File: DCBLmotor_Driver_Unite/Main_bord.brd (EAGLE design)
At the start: 160 x 100 mm, 50 parts, among them CN1 DF11-16DP-2DSA, CN2 DF11-16DP-2DSA, CN3 DF11-4DS-2C, CN4 HIF3FC-10PA-2.54DSA(71), CN5 HIF3FC-10PA-2.54DSA(71), IC1 TMPM370FYFG, IC2 MCP2561FD-E/MF, IC3 AM26C32CD, IC4 AM26C32CD, SW1 CVS-02TB

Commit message: Mount Encoder parts
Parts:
- moved DC11 6.19 mm to (67.8, 65.2)
- moved CN4 5.95 mm to (72.0, 68.8)
- moved CN5 5.80 mm to (72.0, 88.9)
- moved DC12 5.80 mm to (67.8, 85.3)
- moved R2 1.58 mm to (9.65, 72.2), turned to 180 degrees
- moved RA1 1.50 mm to (11.7, 80.0)
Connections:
- net ENC_A-1: now also IC3.3
- net ENC_A-2: now also IC4.3
- net ENC_B-1: now also IC3.5
- net ENC_B-2: now also IC4.5
- net ENC_Z-1: now also IC3.11
- net ENC_Z-2: now also IC4.11
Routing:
- net +5V: track 128.2 -> 78.9 mm, vias 10 -> 9
- net N$36: track 20.2 -> 13.5 mm
- net 1_I2: track 19.7 -> 13.4 mm
- net 2_B1: track 11.8 -> 6.06 mm
- net 1_B1: track 11.5 -> 5.96 mm
- net 2_B2: track 15.2 -> 9.84 mm
- net 1_B2: track 14.0 -> 9.14 mm
- net 2_A2: track 11.4 -> 7.58 mm
- net DIP8: track 31.5 -> 28.4 mm
- net 1_A1: track 7.79 -> 4.81 mm
- net 2_A1: track 7.57 -> 4.60 mm
- net 1_A2: track 10.7 -> 7.90 mm
- net N$35: track 12.8 -> 10.4 mm
- net 1_I1: track 12.6 -> 10.3 mm
- net DIP4: track 21.6 -> 23.9 mm
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
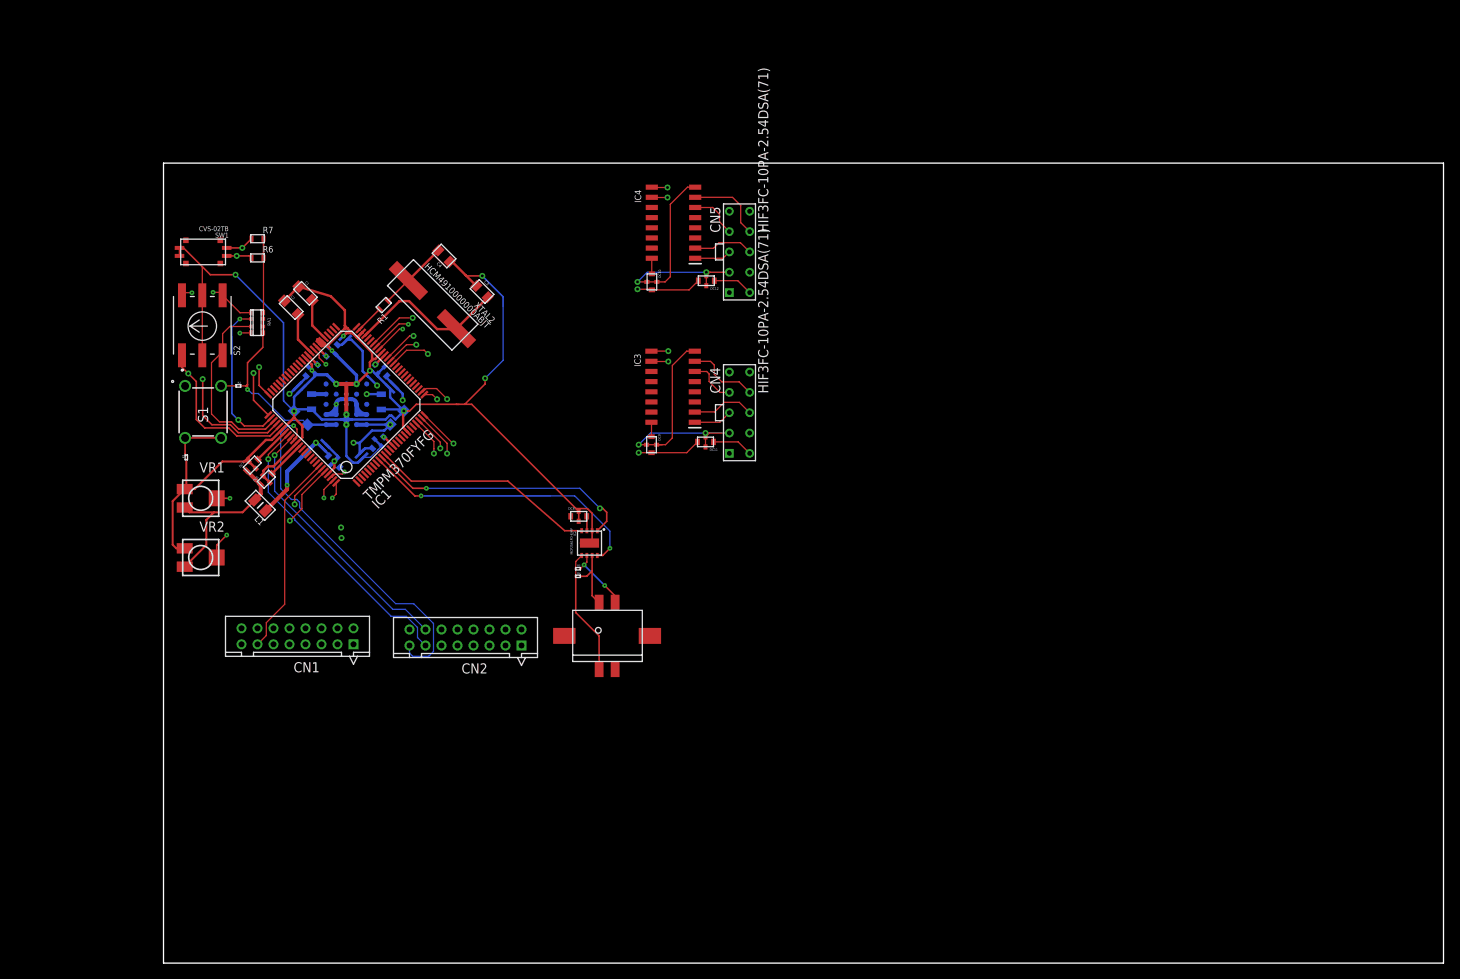
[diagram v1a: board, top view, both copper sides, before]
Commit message: Mount new parts
mount 
holl conecter
change
reset switch
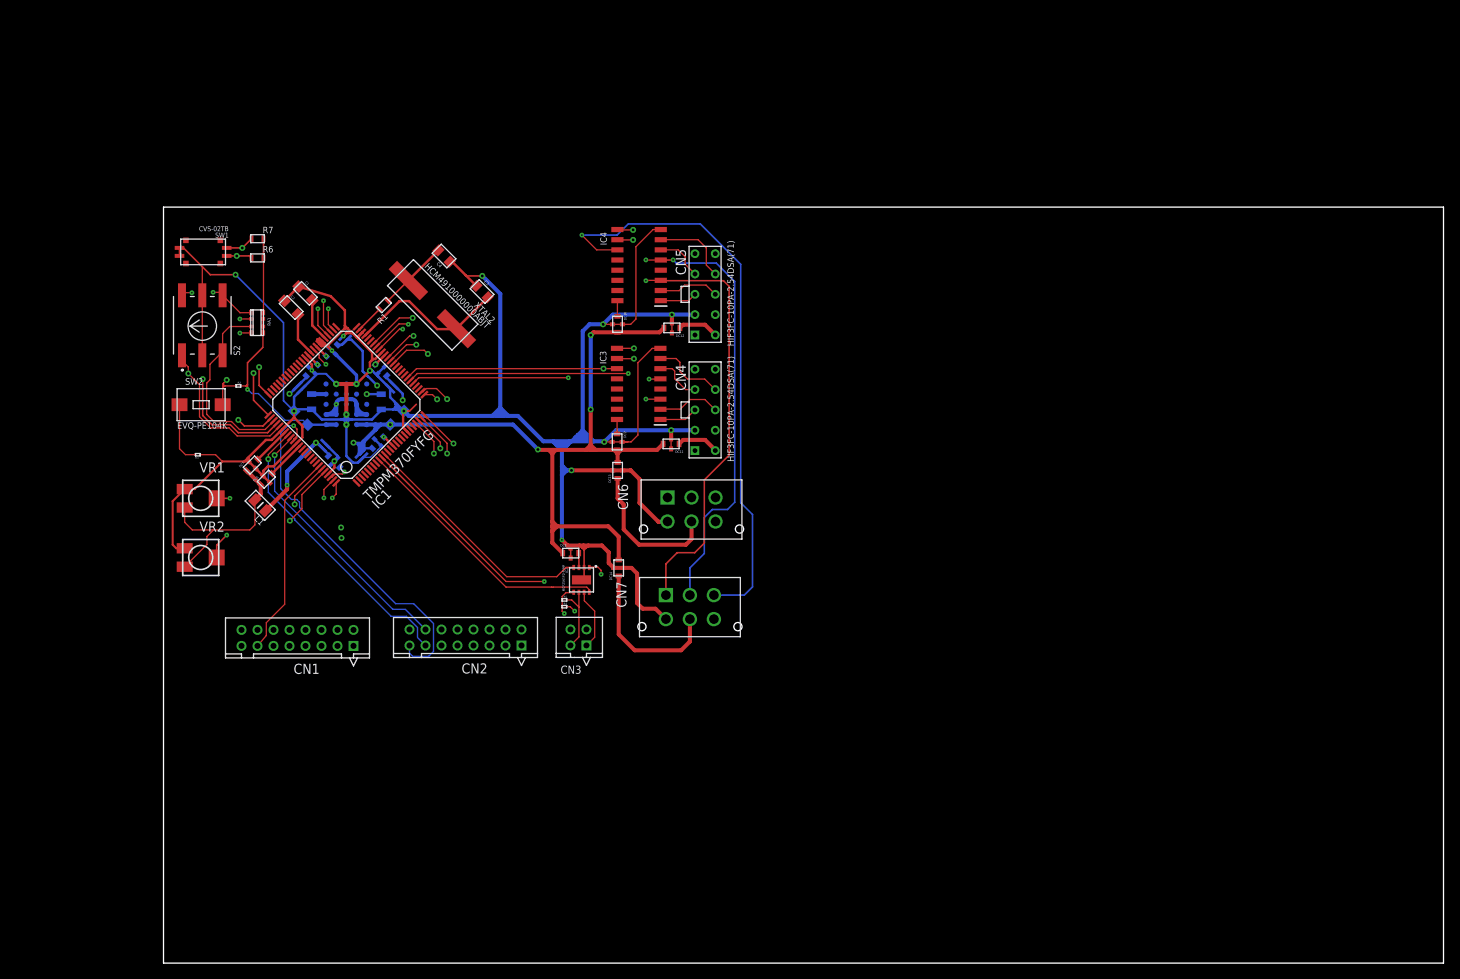
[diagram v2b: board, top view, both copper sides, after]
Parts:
- removed S1: 1825910-6, 1825910-6:1825910-6
- added CN6, CN7: 0430450612, Molex:0430450612
- added DC13, DC14: YFF21PC, TDK:YFF21PC
- added SW2: EVQ-PE104K, Panasonic:EVQ
- CN3: value DF11-4DS-2C -> DF11-4DP-2DSR; device Hirose:DF11-4DS-2C -> Hirose:DF11_4DP-2D
- moved DC12 7.30 mm to (63.5, 79.4)
- moved CN5 6.82 mm to (67.7, 83.6)
- moved DC10 6.82 mm to (56.8, 79.8)
- moved IC4 6.82 mm to (59.5, 87.2)
- moved DC8 4.71 mm to (50.9, 51.2)
- moved IC2 4.71 mm to (52.2, 47.9)
- moved IC3 4.31 mm to (59.4, 72.4)
- moved CN4 4.31 mm to (67.7, 69.2)
- moved DC9 4.31 mm to (56.7, 65.2)
- moved DC11 4.31 mm to (63.5, 64.9)
- moved R5 4.25 mm to (50.4, 45.4)
- moved R4 4.16 mm to (50.4, 44.5)
- moved CN3 3.55 mm to (51.9, 40.9), turned to 0 degrees
- moved R3 1.15 mm to (4.00, 63.5), turned to 0 degrees
- moved CN1 0.20 mm to (23.8, 39.6)
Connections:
- new net N$32: CN6.P$5, DC13.P$2
- new net N$33: CN7.P$5, DC14.P$2
- net +5V: now also DC13.P$1, DC14.P$1
- net ENC_A-1: now also CN6.P$1
- net ENC_A-2: now also CN7.P$1
- net ENC_B-1: now also CN6.P$2
- net ENC_B-2: now also CN7.P$2
- net ENC_Z-1: now also CN6.P$3
- net ENC_Z-2: now also CN7.P$3
- net GND: now also CN6.P$4, CN7.P$4, DC13.GND1, DC13.GND2, DC14.GND1, DC14.GND2
- net N$12: now also SW2.P$1; no longer S1.3, S1.4
- net RESET: now also SW2.P$2; no longer S1.2
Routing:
- net ENC_Z-2: track 0.00 -> 116.8 mm, vias 0 -> 2
- net ENC_B-2: track 0.00 -> 105.2 mm, vias 0 -> 3
- net ENC_A-2: track 0.00 -> 103.6 mm, vias 0 -> 2
- net +5V: track 78.9 -> 157.7 mm, vias 9 -> 10
- net GND: track 322.9 -> 399.6 mm, vias 13 -> 14
- net ENC_Z-1: track 0.00 -> 55.6 mm, vias 0 -> 1
- net ENC_B-1: track 0.00 -> 51.3 mm, vias 0 -> 2
- net ENC_A-1: track 0.00 -> 46.7 mm, vias 0 -> 2
- net N$33: track 0.00 -> 20.3 mm
- net N$32: track 0.00 -> 18.4 mm
- net SPLT: track 15.8 -> 7.59 mm, vias 0 -> 1
- net CANH: track 8.02 -> 14.0 mm, vias 0 -> 1
- net STBY: track 36.6 -> 33.3 mm, vias 2 -> 0
- net RESET: track 19.2 -> 22.5 mm, vias 1 -> 2
- net TX0: track 33.7 -> 36.6 mm
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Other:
- board size 160 x 100 mm -> 160 x 94.5 mm

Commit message: Version1 per finshed
Per complete Version1
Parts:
- removed XTAL2: HCM4910000000ABJT, Citizen:HCM49
- added 0R1, 0R2: 5106, Keystone:5106JUMP_0805
- added C5: T356L107K016AT, KEMET:T356
- added CN10: (no value), jst-xh:B2B-XH-A
- added CN8: BM11B-SRSS-TB, JST:BM11B-SRSS-TB
- added CN9: (no value), jst-xh:B4B-XH-A
- added CR10, CR11, CR12, CR5, CR6, CR7, CR8: NSI50010YT1G, ON Semiconductor:SOD-123
- added DC15: YFF15PC1C104MT000N, TDK:YFF15PC
- added IC5: LTC2862A, LT:DD_PACKGE_8
- added LED1, LED2: CL-340T-SD-T, Citizen:CL-340
- added LED3: CL-196YG-CD-T, Citizen:CL-196
- added R8: MCR006, ROHM:MCR006
- added XTAL1: HCM4910000000ABJT, Citizen:HCM49
- DC6, DC7, DC8: value YFF21PC -> YFF15PC1C104MT000N; device TDK:YFF21PC -> TDK:YFF15PC
- moved VR2 4.65 mm to (4.62, 55.4)
- moved VR1 3.17 mm to (4.65, 61.3)
- moved R7 2.10 mm to (12.5, 92.7)
- moved R6 2.10 mm to (12.5, 90.2)
- moved DC6 2.09 mm to (14.7, 61.5)
- moved DC7 1.95 mm to (12.3, 63.8)
- moved R3 1.83 mm to (4.10, 65.4)
- moved C4 1.25 mm to (35.0, 88.0)
- moved CN1 1.18 mm to (24.9, 39.7)
- moved C3 0.60 mm to (39.9, 83.2)
- moved DC8 0.50 mm to (50.9, 50.8)
- moved C2 0.42 mm to (17.1, 81.4)
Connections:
- new net A*: CN9.3, IC5.P$6, R8.P$2
- new net B*: CN9.4, IC5.P$7, R8.P$1
- new net LED1_1: CR6.P$C, IC1.P$12
- new net LED1_2: CR12.P$C, IC1.P$13
- new net LED1_3: CR7.P$C, IC1.P$15
- new net LED2_1: CR10.P$C, IC1.P$16
- new net LED2_2: CR11.P$C, IC1.P$17
- new net LED2_3: CR8.P$C, IC1.P$18
- new net N$34: CR5.P$A, LED3.P$C
- new net N$37: CR7.P$A, LED1.P$4
- new net N$38: CR12.P$A, LED1.P$5
- new net N$39: CR6.P$A, LED1.P$6
- new net N$40: CR8.P$A, LED2.P$4
- new net N$41: CR11.P$A, LED2.P$5
- new net N$42: CR10.P$A, LED2.P$6
- new net N$43: DC15.P$1, IC5.P$8
- new net N$44: 0R2.P$1, CN9.2
- new net N$46: 0R1.P$1, CN9.1
- net +5V: now also 0R2.P$2, DC15.P$2
- net GND: now also 0R1.P$2, C5.P$-, CN10.2, CR5.P$C, DC15.P$3, DC15.P$4, DC6.P$3, DC6.P$4, DC7.P$3, DC7.P$4, DC8.P$3, DC8.P$4, IC5.P$5, IC5.PAD; no longer DC6.GND1, DC6.GND2, DC7.GND1, DC7.GND2, DC8.GND1, DC8.GND2
- net N$11: now also XTAL1.P$2; no longer XTAL2.P$2
- net N$18: now also CN8.P$5
- net N$19: now also CN8.P$6
- net N$20: now also CN8.P$9
- net N$21: now also CN8.P$7
- net N$22: now also CN8.P$8
- net N$23: now also CN8.P$4
- net N$24: now also CN8.P$3
- net N$25: now also CN8.P$2
- net RESET: now also CN8.P$10
- net RX0: now also IC5.P$4
- net TX0: now also IC5.P$1
- net VCC: now also CN8.P$1, LED1.P$1, LED1.P$2, LED1.P$3, LED2.P$1, LED2.P$2, LED2.P$3, LED3.P$A
- net VDD: now also C5.P$+, CN10.1
- net X1: now also XTAL1.P$1; no longer XTAL2.P$1
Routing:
- net GND: track 399.6 -> 471.6 mm, vias 14 -> 16
- net VCC: track 33.8 -> 90.6 mm, vias 1 -> 2
- net LED2_1: track 0.00 -> 44.9 mm, vias 0 -> 2
- net LED1_1: track 0.00 -> 42.1 mm, vias 0 -> 2
- net LED2_2: track 0.00 -> 41.2 mm, vias 0 -> 2
- net LED1_2: track 0.00 -> 38.8 mm, vias 0 -> 2
- net LED2_3: track 0.00 -> 37.7 mm, vias 0 -> 2
- net LED1_3: track 0.00 -> 36.3 mm, vias 0 -> 2
- net N$25: track 0.00 -> 19.4 mm
- net RX0: track 30.4 -> 49.7 mm, vias 0 -> 2
- net N$24: track 0.00 -> 19.0 mm
- net N$23: track 0.00 -> 18.7 mm
- net N$19: track 0.00 -> 17.9 mm, vias 0 -> 2
- net N$39: track 0.00 -> 17.6 mm
- net N$18: track 0.00 -> 17.6 mm, vias 0 -> 2
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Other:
- board size 160 x 94.5 mm -> 78.4 x 65.5 mm
- board text added: "+"
- board text added: "CAN FD"
- board text added: "ENC 1"
- board text added: "ENC 2"
- board text added: "Hall 1"
- board text added: "Hall 2"
- board text added: "MAX +20V"
- board text added: "Motor 1"
- board text added: "Motor 2"
- board text added: "Pilot LED"
- board text added: "Prototype ONE"
- board text added: "RS485"
- board text added: "RS485 Power jumper"
- board text added: "UESR LED"
